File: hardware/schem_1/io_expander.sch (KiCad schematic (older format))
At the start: 9 parts, among them SW4 DOWN, SW5 UP, SW6 OK, U8 MCP23017_SO

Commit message: Replace ESP32 Wroom module with WRover and remove the external PSRAM (as Wrover has one built in). Create symbol and footprint for Wrover. Update footprints for resistors and buttons. Update USB footprint as it was not matching symbol.
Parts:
- R22, R23, R24, R25: footprint (none) -> Resistor_SMD:R_0603_1608Metric
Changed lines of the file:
@@
 F 0 "R24" H 1459 2371 50  0000 L CNN
 F 1 "2k2" H 1459 2280 50  0000 L CNN
-F 2 "" H 1400 2325 50  0001 C CNN
+F 2 "Resistor_SMD:R_0603_1608Metric" H 1400 2325 50  0001 C CNN
 F 3 "~" H 1400 2325 50  0001 C CNN
 	1    1400 2325
@@
 F 0 "R22" H 6284 1846 50  0000 L CNN
 F 1 "100k" H 6284 1755 50  0000 L CNN
-F 2 "" H 6225 1800 50  0001 C CNN
+F 2 "Resistor_SMD:R_0603_1608Metric" H 6225 1800 50  0001 C CNN
 F 3 "~" H 6225 1800 50  0001 C CNN
 	1    6225 1800
@@
 F 0 "R23" H 6284 2346 50  0000 L CNN
 F 1 "150k" H 6284 2255 50  0000 L CNN
-F 2 "" H 6225 2300 50  0001 C CNN
+F 2 "Resistor_SMD:R_0603_1608Metric" H 6225 2300 50  0001 C CNN
 F 3 "~" H 6225 2300 50  0001 C CNN
 	1    6225 2300
@@
 F 0 "R25" H 4159 2921 50  0000 L CNN
 F 1 "220" H 4159 2830 50  0000 L CNN
-F 2 "" H 4100 2875 50  0001 C CNN
+F 2 "Resistor_SMD:R_0603_1608Metric" H 4100 2875 50  0001 C CNN
 F 3 "~" H 4100 2875 50  0001 C CNN
 	1    4100 2875

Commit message: change supercap for one with lower esr and shorter. create footprint and 3d model for new cap. remove power switch entirely.
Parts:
- SW4, SW5, SW6: footprint Button_Switch_THT:SW_Tactile_SPST_Angled_PTS645Vx31-2LFS -> Digikey:Switch_Tactile_SMD_6x6mm_PTS645
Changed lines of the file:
@@
 F 0 "SW5" H 9575 2535 50  0000 C CNN
 F 1 "UP" H 9575 2444 50  0000 C CNN
-F 2 "Button_Switch_THT:SW_Tactile_SPST_Angled_PTS645Vx31-2LFS" H 9575 2450 50  0001 C CNN
+F 2 "Digikey:Switch_Tactile_SMD_6x6mm_PTS645" H 9575 2450 50  0001 C CNN
 F 3 "~" H 9575 2450 50  0001 C CNN
 	1    9575 2250
@@
 F 0 "SW6" H 9575 2935 50  0000 C CNN
 F 1 "OK" H 9575 2844 50  0000 C CNN
-F 2 "Button_Switch_THT:SW_Tactile_SPST_Angled_PTS645Vx31-2LFS" H 9575 2850 50  0001 C CNN
+F 2 "Digikey:Switch_Tactile_SMD_6x6mm_PTS645" H 9575 2850 50  0001 C CNN
 F 3 "~" H 9575 2850 50  0001 C CNN
 	1    9575 2650
@@
 F 0 "SW4" H 9550 2135 50  0000 C CNN
 F 1 "DOWN" H 9550 2044 50  0000 C CNN
-F 2 "Button_Switch_THT:SW_Tactile_SPST_Angled_PTS645Vx31-2LFS" H 9550 2050 50  0001 C CNN
+F 2 "Digikey:Switch_Tactile_SMD_6x6mm_PTS645" H 9550 2050 50  0001 C CNN
 F 3 "~" H 9550 2050 50  0001 C CNN
 	1    9550 1850

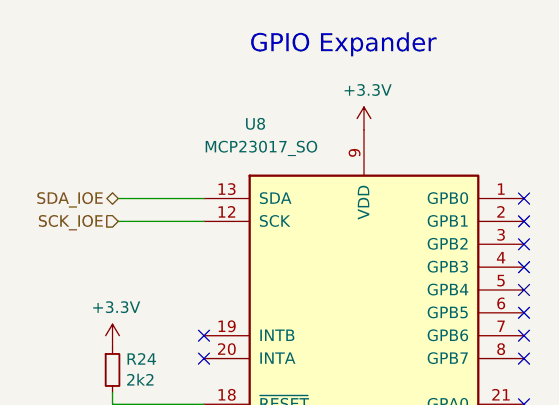
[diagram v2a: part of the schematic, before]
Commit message: update footprints for 24way connector, 3D models. add new connector to connect the two PCB's
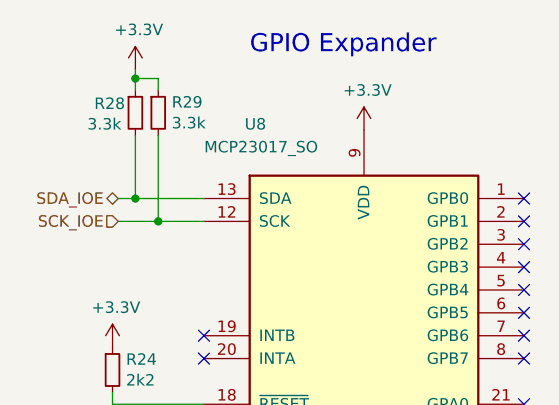
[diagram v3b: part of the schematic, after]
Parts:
- added R28, R29: 3.3k, Resistor_SMD:R_0603_1608Metric, symbol Device:R_Small
- SW4, SW5, SW6: footprint Digikey:Switch_Tactile_SMD_6x6mm_PTS645 -> kicad_lib:JC_Switch_TL6330
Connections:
- wire segments 31 -> 39
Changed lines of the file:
@@
 $EndComp
 Wire Wire Line
-	1800 1675 1425 1675
+	1800 1675 1600 1675
 Text HLabel 1425 1575 0    50   BiDi ~ 0
 SDA_IOE
@@
 NoConn ~ 1800 2175
 NoConn ~ 1800 2275
-Wire Wire Line
-	1800 1575 1425 1575
 $Comp
 L power:+3.3V #PWR044
@@
 F 0 "SW5" H 9575 2535 50  0000 C CNN
 F 1 "UP" H 9575 2444 50  0000 C CNN
-F 2 "Digikey:Switch_Tactile_SMD_6x6mm_PTS645" H 9575 2450 50  0001 C CNN
+F 2 "kicad_lib:JC_Switch_TL6330" H 9575 2450 50  0001 C CNN
 F 3 "~" H 9575 2450 50  0001 C CNN
 	1    9575 2250
@@
 F 0 "SW6" H 9575 2935 50  0000 C CNN
 F 1 "OK" H 9575 2844 50  0000 C CNN
-F 2 "Digikey:Switch_Tactile_SMD_6x6mm_PTS645" H 9575 2850 50  0001 C CNN
+F 2 "kicad_lib:JC_Switch_TL6330" H 9575 2850 50  0001 C CNN
 F 3 "~" H 9575 2850 50  0001 C CNN
 	1    9575 2650
@@
 F 0 "SW4" H 9550 2135 50  0000 C CNN
 F 1 "DOWN" H 9550 2044 50  0000 C CNN
-F 2 "Digikey:Switch_Tactile_SMD_6x6mm_PTS645" H 9550 2050 50  0001 C CNN
+F 2 "kicad_lib:JC_Switch_TL6330" H 9550 2050 50  0001 C CNN
 F 3 "~" H 9550 2050 50  0001 C CNN
 	1    9550 1850
 	1    0    0    -1
 $EndComp
+$Comp
+L Device:R_Small R28
+U 1 1 60CFBD78
+P 1500 1200
+F 0 "R28" H 1320 1240 50  0000 L CNN
+F 1 "3.3k" H 1290 1150 50  0000 L CNN
+F 2 "Resistor_SMD:R_0603_1608Metric" H 1500 1200 50  0001 C CNN
+F 3 "~" H 1500 1200 50  0001 C CNN
+	1    1500 1200
+	1    0    0    -1
+$EndComp
+$Comp
+L power:+3.3V #PWR0104
+U 1 1 60CFC6D7
+P 1500 1010
+F 0 "#PWR0104" H 1500 860 50  0001 C CNN
+F 1 "+3.3V" H 1515 1183 50  0000 C CNN
+F 2 "" H 1500 1010 50  0001 C CNN
+F 3 "" H 1500 1010 50  0001 C CNN
+	1    1500 1010
+	1    0    0    -1
+$EndComp
+Wire Wire Line
+	1425 1575 1500 1575
+Wire Wire Line
+	1500 1300 1500 1575
+Connection ~ 1500 1575
+Wire Wire Line
+	1500 1575 1800 1575
+$Comp
+L Device:R_Small R29
+U 1 1 60D01229
+P 1600 1200
+F 0 "R29" H 1659 1246 50  0000 L CNN
+F 1 "3.3k" H 1659 1155 50  0000 L CNN
+F 2 "Resistor_SMD:R_0603_1608Metric" H 1600 1200 50  0001 C CNN
+F 3 "~" H 1600 1200 50  0001 C CNN
+	1    1600 1200
+	1    0    0    -1
+$EndComp
+Wire Wire Line
+	1600 1300 1600 1675
+Connection ~ 1600 1675
+Wire Wire Line
+	1600 1675 1425 1675
+Wire Wire Line
+	1500 1010 1500 1050
+Wire Wire Line
+	1600 1100 1600 1050
+Wire Wire Line
+	1600 1050 1500 1050
+Connection ~ 1500 1050
+Wire Wire Line
+	1500 1050 1500 1100
 $EndSCHEMATC

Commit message: update to latest gerbers, update project plan
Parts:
- D4: LCSC (none) -> C84256
- R22: LCSC (none) -> C25803
- R23: LCSC (none) -> C22807
- R24: LCSC (none) -> C125931
- R25: LCSC (none) -> C22962
- R28, R29: LCSC (none) -> C22978
- U8: LCSC (none) -> C47023
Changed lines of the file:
@@
 F 2 "Package_SO:SOIC-28W_7.5x17.9mm_P1.27mm" H 2700 1375 50  0001 L CNN
 F 3 "http://ww1.microchip.com/downloads/en/DeviceDoc/20001952C.pdf" H 2700 1275 50  0001 L CNN
+F 4 "C47023" H 2500 2375 50  0001 C CNN "LCSC"
 	1    2500 2375
 	1    0    0    -1
@@
 F 2 "Resistor_SMD:R_0603_1608Metric" H 1400 2325 50  0001 C CNN
 F 3 "~" H 1400 2325 50  0001 C CNN
+F 4 "C125931" H 1400 2325 50  0001 C CNN "LCSC"
 	1    1400 2325
 	1    0    0    -1
@@
 F 2 "Resistor_SMD:R_0603_1608Metric" H 6225 1800 50  0001 C CNN
 F 3 "~" H 6225 1800 50  0001 C CNN
+F 4 "C25803" H 6225 1800 50  0001 C CNN "LCSC"
 	1    6225 1800
 	1    0    0    -1
@@
 F 2 "Resistor_SMD:R_0603_1608Metric" H 6225 2300 50  0001 C CNN
 F 3 "~" H 6225 2300 50  0001 C CNN
+F 4 "C22807" H 6225 2300 50  0001 C CNN "LCSC"
 	1    6225 2300
 	1    0    0    -1
@@
 F 2 "LED_SMD:LED_0805_2012Metric" H 4100 3125 50  0001 C CNN
 F 3 "~" H 4100 3125 50  0001 C CNN
+F 4 "C84256" V 4100 3125 50  0001 C CNN "LCSC"
 	1    4100 3125
 	0    -1   -1   0
@@
 F 2 "Resistor_SMD:R_0603_1608Metric" H 4100 2875 50  0001 C CNN
 F 3 "~" H 4100 2875 50  0001 C CNN
+F 4 "C22962" H 4100 2875 50  0001 C CNN "LCSC"
 	1    4100 2875
 	1    0    0    -1
@@
 F 2 "Resistor_SMD:R_0603_1608Metric" H 1500 1200 50  0001 C CNN
 F 3 "~" H 1500 1200 50  0001 C CNN
+F 4 "C22978" H 1500 1200 50  0001 C CNN "LCSC"
 	1    1500 1200
 	1    0    0    -1
@@
 F 2 "Resistor_SMD:R_0603_1608Metric" H 1600 1200 50  0001 C CNN
 F 3 "~" H 1600 1200 50  0001 C CNN
+F 4 "C22978" H 1600 1200 50  0001 C CNN "LCSC"
 	1    1600 1200
 	1    0    0    -1

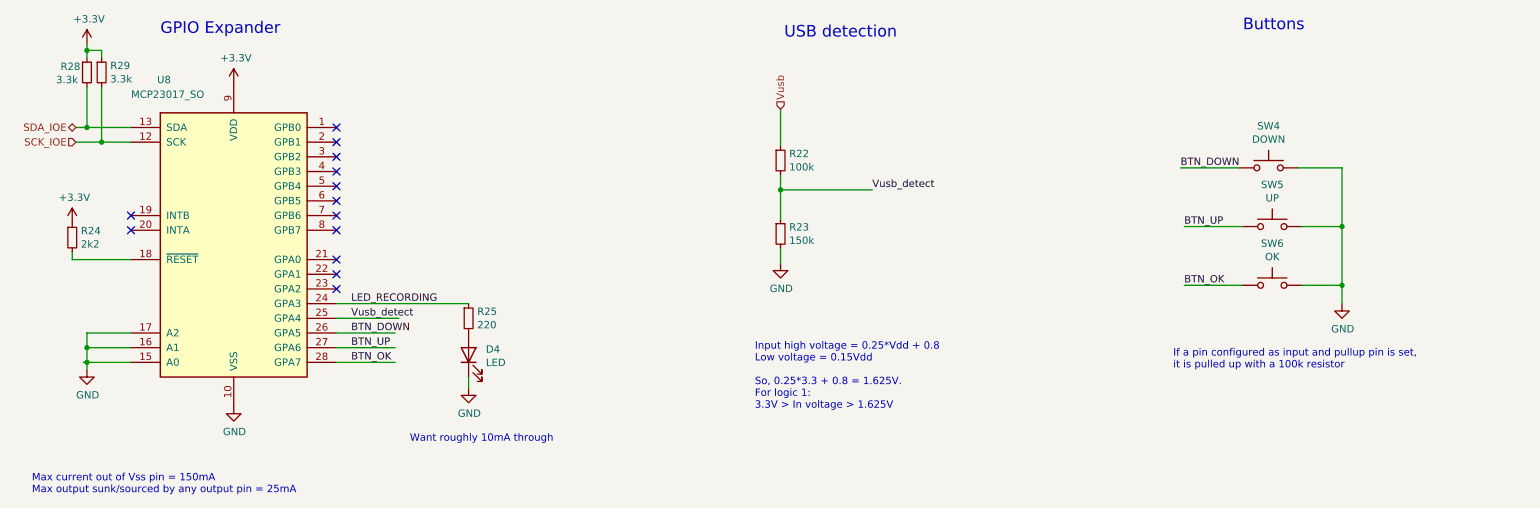
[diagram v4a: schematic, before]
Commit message: move old production stuff to new folder. start pcb spin 2: add test points (smd and pads). add third diode as currently disconnected USB can not be detected. increase LED resistor values are too bright. improve OLED footprint (to accomodate inaccuracies in drawing).
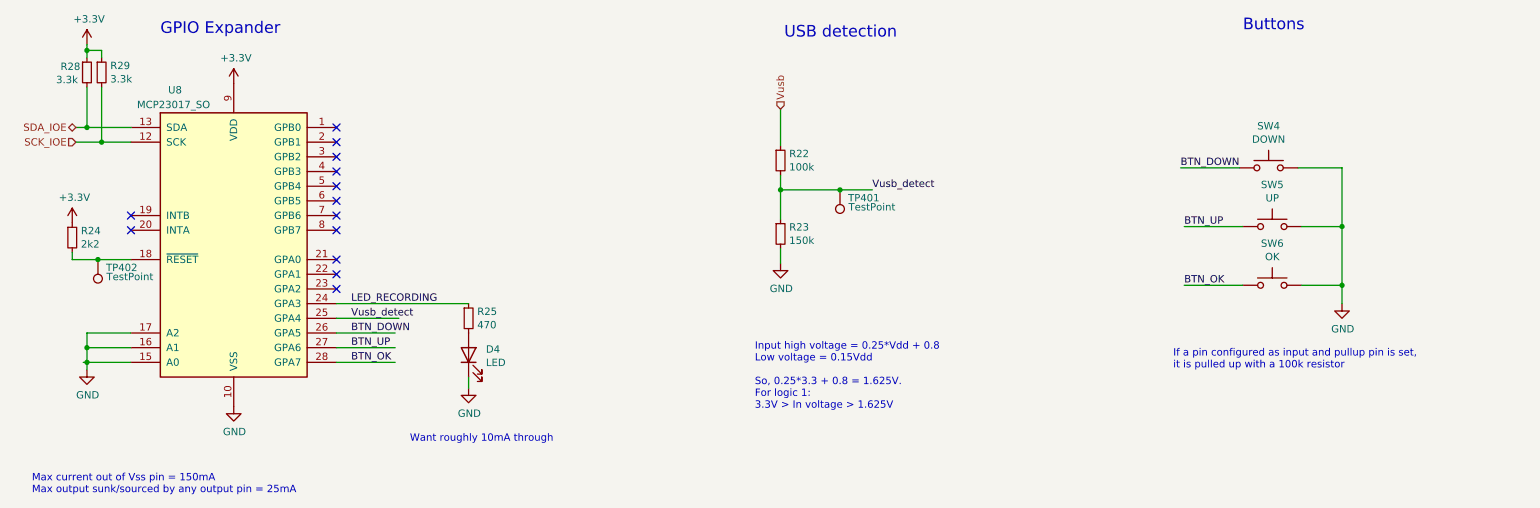
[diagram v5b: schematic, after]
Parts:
- added TP401, TP402: TestPoint, TestPoint:TestPoint_Pad_2.0x2.0mm, symbol Connector:TestPoint
- R25: value 220 -> 470
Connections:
- wire segments 39 -> 41
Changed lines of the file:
@@
 U 1 1 60ABCEFB
 P 2500 2375
-F 0 "U8" H 2025 3500 50  0000 C CNN
-F 1 "MCP23017_SO" H 2050 3400 50  0000 C CNN
+F 0 "U8" H 2100 3430 50  0000 C CNN
+F 1 "MCP23017_SO" H 2090 3330 50  0000 C CNN
 F 2 "Package_SO:SOIC-28W_7.5x17.9mm_P1.27mm" H 2700 1375 50  0001 L CNN
 F 3 "http://ww1.microchip.com/downloads/en/DeviceDoc/20001952C.pdf" H 2700 1275 50  0001 L CNN
@@
 $EndComp
 Wire Wire Line
-	1800 2475 1400 2475
+	1800 2475 1575 2475
 Wire Wire Line
 	1400 2475 1400 2425
@@
 Input high voltage = 0.25*Vdd + 0.8\nLow voltage = 0.15Vdd\n\nSo, 0.25*3.3 + 0.8 = 1.625V.\nFor logic 1:\n3.3V > In voltage > 1.625V
 Wire Wire Line
-	6225 2000 6850 2000
+	6225 2000 6630 2000
 Text Notes 8900 3225 0    50   ~ 0
 If a pin configured as input and pullup pin is set,\nit is pulled up with a 100k resistor
@@
 P 4100 2875
 F 0 "R25" H 4159 2921 50  0000 L CNN
-F 1 "220" H 4159 2830 50  0000 L CNN
+F 1 "470" H 4159 2830 50  0000 L CNN
 F 2 "Resistor_SMD:R_0603_1608Metric" H 4100 2875 50  0001 C CNN
 F 3 "~" H 4100 2875 50  0001 C CNN
@@
 Wire Wire Line
 	1500 1050 1500 1100
+$Comp
+L Connector:TestPoint TP401
+U 1 1 61459396
+P 6630 2000
+F 0 "TP401" H 6575 2055 50  0000 R CNN
+F 1 "TestPoint" H 6572 2117 50  0000 R CNN
+F 2 "TestPoint:TestPoint_Pad_2.0x2.0mm" H 6830 2000 50  0001 C CNN
+F 3 "~" H 6830 2000 50  0001 C CNN
+	1    6630 2000
+	-1   0    0    1
+$EndComp
+Connection ~ 6630 2000
+Wire Wire Line
+	6630 2000 6850 2000
+$Comp
+L Connector:TestPoint TP402
+U 1 1 614C2D87
+P 1575 2475
+F 0 "TP402" H 1520 2530 50  0000 R CNN
+F 1 "TestPoint" H 1517 2592 50  0000 R CNN
+F 2 "TestPoint:TestPoint_Pad_2.0x2.0mm" H 1775 2475 50  0001 C CNN
+F 3 "~" H 1775 2475 50  0001 C CNN
+	1    1575 2475
+	-1   0    0    1
+$EndComp
+Connection ~ 1575 2475
+Wire Wire Line
+	1575 2475 1400 2475
 $EndSCHEMATC
